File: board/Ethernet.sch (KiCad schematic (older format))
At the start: 48 parts, among them J6 GBE_RJ45_MAG, U20 KSZ9031RNX, U23 24AA02E48, X2 25MHz

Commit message: Issue #1481 - DOC
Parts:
- removed C210, C235, C238, C239: 100nF, ~, symbol C
- removed GS1: GS2, symbol GS2
- removed J6: GBE_RJ45_MAG, GBE_RJ45_MAG, symbol GBE_RJ45_MAG
- removed L10, L6, L9: INDUCTOR, ~, symbol INDUCTOR
- removed R218, R219, R220: 4.7K, ~, symbol R
- removed R221: 12.1K, ~, symbol R
- removed R222, R223: 10K, ~, symbol R
- removed R224, R225: 220R, ~, symbol R
- removed U20: KSZ9031RNX, ~, symbol KSZ9031RNX
- added C203: 4.7uF, symbol C
- added C204: 1uF, symbol C
- added C226, C229, C232: 100nF, ~, symbol C
- added J6: RJ45(HFJ11-1GO1ERL), ~, symbol RJ45(HFJ11-1GO1ERL)
- added L1: INDUCTOR, ~, symbol INDUCTOR
- added R38: 39K, ~, symbol R
- added R39: 27K, ~, symbol R
- added R48, R49, R51, R65, R66, R67, R71, R74, R75: 4.7K, ~, symbol R
- added R50: 1.5K, ~, symbol R
- added R69: 2.49K, ~, symbol R
- added R70, R73: 390R, ~, symbol R
- added R72: 0R, ~, symbol R
- added R89, R92: 330R, ~, symbol R
- added U19: MCP1825, ~, symbol MCP1825
- added U20: RTL8211E-VB, ~, symbol RTL8211E-VL
- C210: renamed from C230; value 100nF -> 4.7uF
- C211, C212, C225: value 100nF -> 4.7uF
- C216: value 100nF -> 27pF
- C220: value 4.7uF -> 100nF
- C222: value 100nF -> 0.1uF
- R22: value 4.7K -> 1K
- X2: value 25MHz -> 50MHz
- renumbered C226 to C227, C227 to C228, C228 to C230, C229 to C231, C231 to C235, C232 to C238, C240 to C239, L8 to L6, R226 to R116, R227 to R93
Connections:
- net labels added: AVDD3V3, ETH_INT_B, ETH_MDC, ETH_MDIO, ETH_RESET_B, ETH_RXCLK, ETH_RXCTL, ETH_RXD0, ETH_RXD1, ETH_RXD2, ETH_RXD3, ETH_RXD[0..3], ETH_TXCLK, ETH_TXCTL, ETH_TXD0, ETH_TXD1, ETH_TXD2, ETH_TXD3, ETH_TXD[0..3], ETH_VCC1V0, ETH_VCC3V3, FPGA_CLK, LED0, SYSCLK, VCC1V0, XTAL1_50MHZ, XTAL2_50MHZ
- net labels removed: AVDDH, AVDDL, CLK125_NDO, C_GND, DVDDH, GTX_CLK, INIT_N, INT_N, LED2, MDC, MDIO, PLL1V2, RESET_B, RXD0, RXD1, RXD2, RXD3, RXD[0..3], RX_CLK, RX_DV, TXD0, TXD1, TXD2, TXD3, TXD[0..3], TX_EN, VCC1V2, XTAL1, XTAL2
- wire segments 195 -> 227
- no-connect marks 1 -> 6
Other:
- note added: "VCC1V0"
- moved on the sheet: C210, C224, C225, C227, C228, C230, C231, C235, C238, C239, L6, R116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

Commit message: Issue #1481 - GPIO sheet
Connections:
- net SYSCLK: no longer names the net of U20.46 (CLK125)
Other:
- note removed: "ETH MAC ADDRESS"
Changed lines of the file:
@@
 LIBS:valves
 LIBS:hdmi2usb
+LIBS:timvideos-pcie-8x
 LIBS:HDMI2USB-cache
-LIBS:Atlys-VHDCI-cache
 EELAYER 27 0
 EELAYER END
 $Descr A3 16535 11693
 encoding utf-8
-Sheet 3 12
+Sheet 11 12
 Title "HDMI2USB"
-Date "18 feb 2015"
+Date "20 feb 2015"
 Rev "Rev2"
 Comp "Numato Lab"
@@
 MAC_SCL
 $Comp
-L GND #PWR04
+L GND #PWR43
 U 1 1 53CC9E90
 P 14600 8600
-F 0 "#PWR04" H 14600 8600 30  0001 C CNN
+F 0 "#PWR43" H 14600 8600 30  0001 C CNN
 F 1 "GND" H 14600 8530 30  0001 C CNN
 F 2 "" H 14600 8600 60  0001 C CNN
@@
 $EndComp
 $Comp
-L GND #PWR05
+L GND #PWR44
 U 1 1 53CC9E9C
 P 15000 8400
-F 0 "#PWR05" H 15000 8400 30  0001 C CNN
+F 0 "#PWR44" H 15000 8400 30  0001 C CNN
 F 1 "GND" H 15000 8330 30  0001 C CNN
 F 2 "" H 15000 8400 60  0001 C CNN
@@
 $EndComp
 $Comp
-L GND #PWR06
+L GND #PWR42
 U 1 1 53CC9EA2
 P 13650 9300
-F 0 "#PWR06" H 13650 9300 30  0001 C CNN
+F 0 "#PWR42" H 13650 9300 30  0001 C CNN
 F 1 "GND" H 13650 9230 30  0001 C CNN
 F 2 "" H 13650 9300 60  0001 C CNN
@@
 Text Label 6300 5200 0    47   ~ 0
 ETH_RESET_B
-Text Label 6450 5750 0    47   ~ 0
-SYSCLK
 $Comp
 L R R51
@@
 $EndComp
 $Comp
-L GND #PWR07
+L GND #PWR41
 U 1 1 54772306
 P 3500 9650
-F 0 "#PWR07" H 3500 9650 30  0001 C CNN
+F 0 "#PWR41" H 3500 9650 30  0001 C CNN
 F 1 "GND" H 3500 9580 30  0001 C CNN
 F 2 "" H 3500 9650 60  0001 C CNN
@@
 Text Notes 2250 7600 0    118  ~ 24
 VCC1V0
-Text Notes 12900 7650 0    118  ~ 24
-ETH MAC ADDRESS
 Text Label 4050 9600 2    60   ~ 0
 GND
@@
 Entry Wire Line
 	6350 4200 6450 4300
-Text HLabel 6250 3900 0    47   Input ~ 0
+Text HLabel 6250 3900 0    47   Output ~ 0
 ETH_TXD[0..3]
 Wire Wire Line
@@
 	6300 5650 6800 5650
 Wire Wire Line
-	6800 5750 6450 5750
-Wire Wire Line
 	6050 5200 6050 5300
 Wire Wire Line
@@
 Wire Bus Line
 	6350 3900 6250 3900
-Text HLabel 6450 4400 0    47   Input ~ 0
+Text HLabel 6450 4400 0    47   Output ~ 0
 ETH_TXCTL
 Text HLabel 4300 2850 0    47   Input ~ 0
@@
 Wire Bus Line
 	4350 2850 4300 2850
-Text HLabel 6450 4500 0    47   Input ~ 0
+Text HLabel 6450 4500 0    47   Output ~ 0
 ETH_TXCLK
 Text HLabel 4450 3800 0    47   Input ~ 0
@@
 Text HLabel 5750 5200 0    47   Input ~ 0
 ETH_RESET_B
-Text HLabel 6450 5750 0    47   Input ~ 0
-SYSCLK
 Text HLabel 11850 8200 2    47   Input ~ 0
 FPGA_CLK
@@
 Text HLabel 14950 8750 2    47   Input ~ 0
 MAC_SCL
-Text HLabel 5700 4700 0    47   Input ~ 0
+Text HLabel 5700 4700 0    47   BiDi ~ 0
 ETH_MDIO
-Text HLabel 14950 8850 2    47   Input ~ 0
+Text HLabel 14950 8850 2    47   BiDi ~ 0
 MAC_SDA
 Connection ~ 5750 4700
@@
 	6050 5700 6050 5850
 NoConn ~ 10750 4600
-NoConn ~ 13800 7150
+NoConn ~ 6800 5750
 $EndSCHEMATC

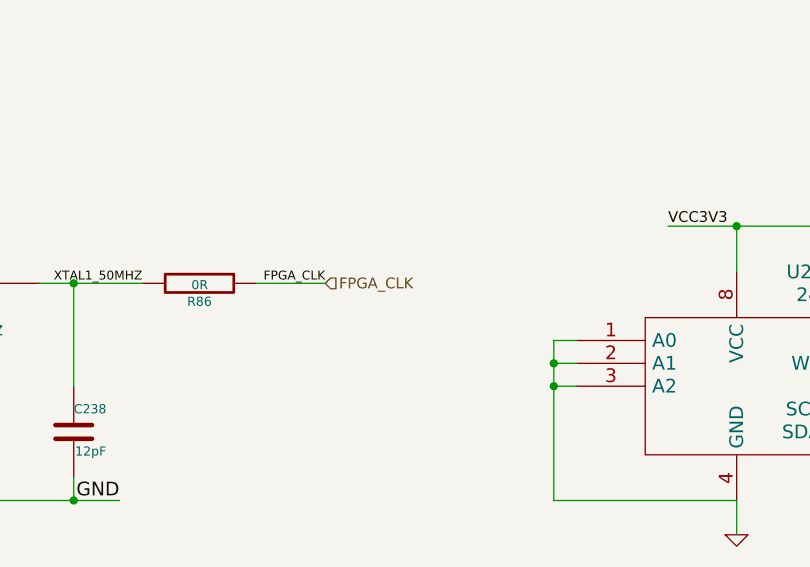
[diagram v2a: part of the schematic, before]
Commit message: Issue #1481 - CYPRESS-FPGA CONNECTIONS ADDED
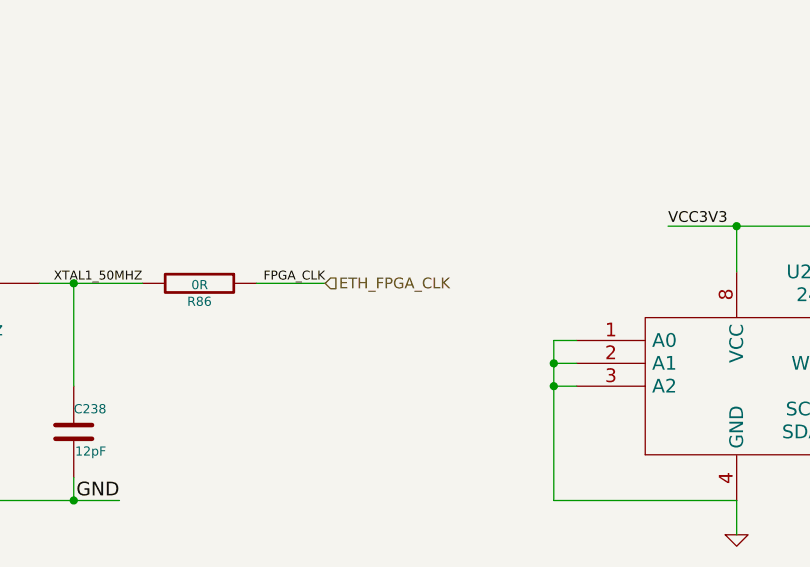
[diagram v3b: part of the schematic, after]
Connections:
- net FPGA_CLK renamed ETH_FPGA_CLK
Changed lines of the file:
@@
 Sheet 11 12
 Title "HDMI2USB"
-Date "20 feb 2015"
+Date "24 feb 2015"
 Rev "Rev2"
 Comp "Numato Lab"
@@
 MAC_SCL
 $Comp
-L GND #PWR43
+L GND #PWR043
 U 1 1 53CC9E90
 P 14600 8600
-F 0 "#PWR43" H 14600 8600 30  0001 C CNN
+F 0 "#PWR043" H 14600 8600 30  0001 C CNN
 F 1 "GND" H 14600 8530 30  0001 C CNN
 F 2 "" H 14600 8600 60  0001 C CNN
@@
 $EndComp
 $Comp
-L GND #PWR44
+L GND #PWR044
 U 1 1 53CC9E9C
 P 15000 8400
-F 0 "#PWR44" H 15000 8400 30  0001 C CNN
+F 0 "#PWR044" H 15000 8400 30  0001 C CNN
 F 1 "GND" H 15000 8330 30  0001 C CNN
 F 2 "" H 15000 8400 60  0001 C CNN
@@
 $EndComp
 $Comp
-L GND #PWR42
+L GND #PWR045
 U 1 1 53CC9EA2
 P 13650 9300
-F 0 "#PWR42" H 13650 9300 30  0001 C CNN
+F 0 "#PWR045" H 13650 9300 30  0001 C CNN
 F 1 "GND" H 13650 9230 30  0001 C CNN
 F 2 "" H 13650 9300 60  0001 C CNN
@@
 $EndComp
 $Comp
-L GND #PWR41
+L GND #PWR046
 U 1 1 54772306
 P 3500 9650
-F 0 "#PWR41" H 3500 9650 30  0001 C CNN
+F 0 "#PWR046" H 3500 9650 30  0001 C CNN
 F 1 "GND" H 3500 9580 30  0001 C CNN
 F 2 "" H 3500 9650 60  0001 C CNN
@@
 ETH_RESET_B
 Text HLabel 11850 8200 2    47   Input ~ 0
-FPGA_CLK
+ETH_FPGA_CLK
 Text HLabel 5700 4800 0    47   Input ~ 0
 ETH_MDC

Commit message: Issue #1605
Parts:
- removed R116, R93: 10K, symbol R
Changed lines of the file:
@@
 Sheet 11 12
 Title "HDMI2USB"
-Date "11 mar 2015"
+Date "12 mar 2015"
 Rev "Rev2"
 Comp "Numato Lab"
@@
 	1    0    0    -1
 $EndComp
-$Comp
-L R R116
-U 1 1 53CC9E82
-P 14900 9150
-F 0 "R116" V 14980 9150 50  0000 C CNN
-F 1 "10K" V 14900 9150 50  0000 C CNN
-F 2 "" H 14900 9150 60  0001 C CNN
-F 3 "" H 14900 9150 60  0001 C CNN
-	1    14900 9150
-	1    0    0    -1
-$EndComp
-$Comp
-L R R93
-U 1 1 53CC9E88
-P 14800 9150
-F 0 "R93" V 14700 9150 50  0000 C CNN
-F 1 "10K" V 14800 9150 50  0000 C CNN
-F 2 "" H 14800 9150 60  0001 C CNN
-F 3 "" H 14800 9150 60  0001 C CNN
-	1    14800 9150
-	1    0    0    -1
-$EndComp
 Text Label 14700 8850 2    47   ~ 0
 MAC_SDA
@@
 $EndComp
 Text Label 13350 7950 0    47   ~ 0
-VCC3V3
-Text Label 15000 9400 0    47   ~ 0
 VCC3V3
 $Comp
@@
 Connection ~ 9900 8200
 Connection ~ 10750 8200
-Connection ~ 14900 9400
-Wire Wire Line
-	15000 9400 14800 9400
 Wire Wire Line
 	14350 8750 14950 8750
@@
 Wire Wire Line
 	5750 4650 5750 4700
-Wire Wire Line
-	14800 8850 14800 8900
-Wire Wire Line
-	14900 8750 14900 8900
-Connection ~ 14900 8750
-Connection ~ 14800 8850
 Connection ~ 5800 5200
 Wire Wire Line
